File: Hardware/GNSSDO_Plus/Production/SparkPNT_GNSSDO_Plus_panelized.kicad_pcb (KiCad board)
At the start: 4 copper layers, 165.6 x 125.5 mm, 478 parts, among them J1 SMA_Edge, J10 SMA_Edge, J2 USB_C_Receptacle, J3 SMA_Edge, J4 USB_C_Receptacle, J5 MagJack_PoE, J6 microSD, J7 Qwiic_Vertical, J8 SMA_Edge, J9 Screw_Cage_3.5mm-10, Q1 MBT3904DW1, Q2 DMG2305UX, Q3 DMG2305UX, Q4 DMG2305UX, Q5 DMG2305UX, Q6 DMG2305UX, Q7 DMG2305UX, Q8 DMG2305UX, Q9 DMG2305UX, SW1 PTH_RA_h7.5mm, SW2 PTH_RA_h7.5mm, SW3 PTH_RA_h7.5mm, SW4 DPDT_Slide_SMD_7.2x3.5mm, U1 ESP32-WROVER-IE-N16R8, U10 74LVC2T45DC, U11 AP7361C-3.3V, U12 74LVC2T45DC, U13 STP3593LF, U14 74LVC2T45DC, U15 SN74LVC1G175DCK, U16 JPS-3-1+, U17 LMV7219M5, U18 MS8607-02BA, U19 PCA9306, U2 mosaic-T, U20 LMV7219M5, U23 LMV7219M5, U24 LMV7219M5, U25 AP2112K-3.3, U26 LTC4418, U27 LTC4418, U3 CH340C, U4 KSZ8041NL/I, U5 AP7361C-3.3V, U6 REC15E-2405SZ, U7 DP5305, U8 74LVC2T45DC, U9 74LVC2T45DC

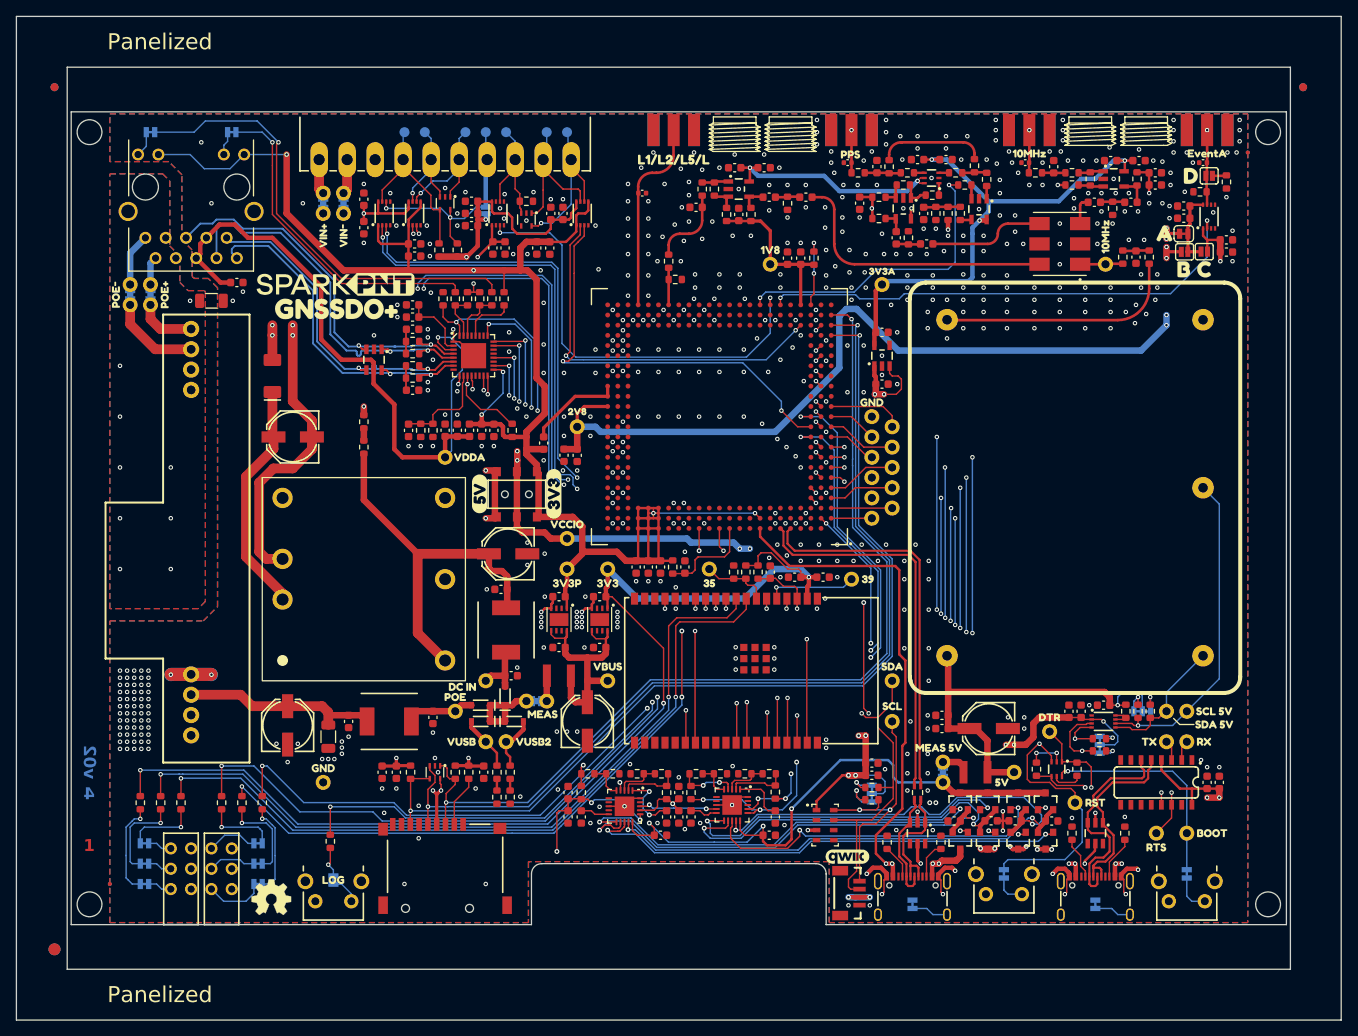
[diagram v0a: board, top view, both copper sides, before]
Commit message: Reduce PCB width by 1.5mm. Bump to v10
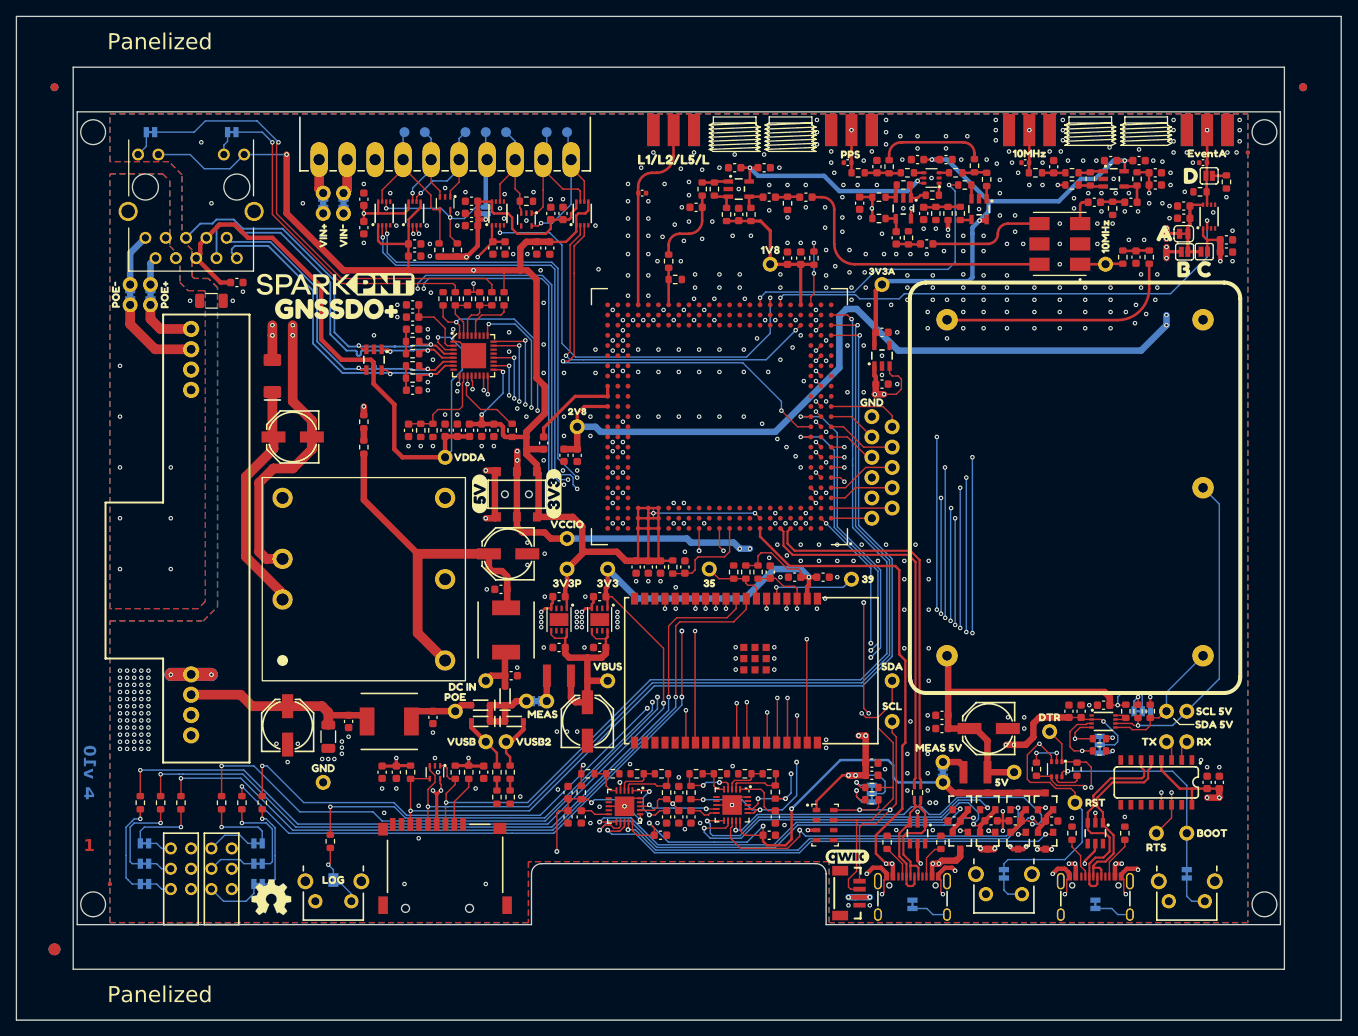
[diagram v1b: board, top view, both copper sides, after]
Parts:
- removed the ? at (255.8, 47.7) (x2)
- removed the ? at (99.8, 47.7) (x2)
- removed the ? at (99.8, 155.5) (x2)
- added ?: , Fiducial_1mm_Mask3mm, F.Cu at (99.8, 47.7)
- added ?: , Fiducial_1.5mm_Mask3mm, F.Cu at (99.8, 155.5)
- added ?: , Fiducial_1mm_Mask3mm, F.Cu at (255.8, 47.7)
- added ?: , Fiducial_1.5mm_Mask3mm, B.Cu at (99.8, 155.5)
- added ?: , Fiducial_1mm_Mask3mm, B.Cu at (255.8, 47.7)
- added ?: , Fiducial_1mm_Mask3mm, B.Cu at (99.8, 47.7)
- C9: value 1nF -> 1.0nF
- J1, J10, J3, J8: footprint SparkFun-Connector:SMA_Edge -> SparkFun-Connector:SMA_Edge_6.3mm
- J7: footprint SparkFun-Connector:JST_SMD_1.0mm-4_Vertical_Black -> SparkFun-Connector:JST_1x04_P1.0mm_Vertical_SMD
- J9: footprint SparkFun-Connector:Screw_Cage_3.5mm-10 -> SparkFun-Connector:ScrewCage_1x10_P3.5mm_Horizontal
- L1, L2: value 470Ohm -> 470 Ohm
- Q1, U15: footprint SparkFun-Semiconductor-Standard:SOT-323 -> SparkFun-Semiconductor-Standard:SOT-363_SC-70-6
- TP1, TP10, TP11, TP12, TP13, TP14, TP15, TP16, TP17, TP18, TP19, TP2, TP21, TP22, TP23, TP24, TP25, TP26, TP27, TP28, TP29, TP3, TP33, TP34, TP35, TP36, TP37, TP38, TP39, TP4, TP40, TP41, TP43, TP5, TP6, TP7, TP8, TP9: footprint SparkFun-Connector:1x01 -> SparkFun-Connector:1x01_P2.54mm
- TR1: footprint SparkFun-Coil:RFCMF1220100M4T -> SparkFun-Coil:Choke_100MHz_USB
- U2: footprint SparkFun-GPS:MOSAIC_LGA -> SparkFun-GNSS:Septentrio_mosaic_LGA
- moved ST1 0.45 mm to (251.0, 53.3)
- moved ST3 0.45 mm to (251.0, 149.9)
- moved ST2 0.45 mm to (104.6, 53.3)
- moved ST4 0.45 mm to (104.6, 149.9)
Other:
- outline, holes or cut-outs redrawn
- board text added: "v10"
- board text removed: "V-Score To V-Score"
- board text removed: "v02"
